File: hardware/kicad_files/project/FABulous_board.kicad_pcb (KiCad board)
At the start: 4 copper layers, 101.2 x 63.5 mm, 87 parts, among them J1 Conn_01x03_Pin, J10 Conn_01x03_Pin, J2 Conn_01x02_Socket, J3 Conn_02x12_Odd_Even, J4 Conn_01x03_Pin, J5 Conn_01x03_Pin, J6 Conn_01x03_Pin, J7 Conn_01x03_Pin, J8 Conn_01x03_Pin, J9 Conn_01x02_Pin, SW1 Tactile Switch, U1 W25Q32FVSS, U10 SN74LVC1G125DCKR, U11 SI5351A-B-GTR, U4 GT-USB-7010ASV, U5 FT232H, U6 AMS1117-3_3, U7 SPX1117M3-L-1-5_TR, U8 MCP1319MT-29LE-OT, U9 SN74LVC1G125DCKR, X1 TXM12M0004252DBCEO00T, X2 NX3225GA-25_000M-STD-CRG-2

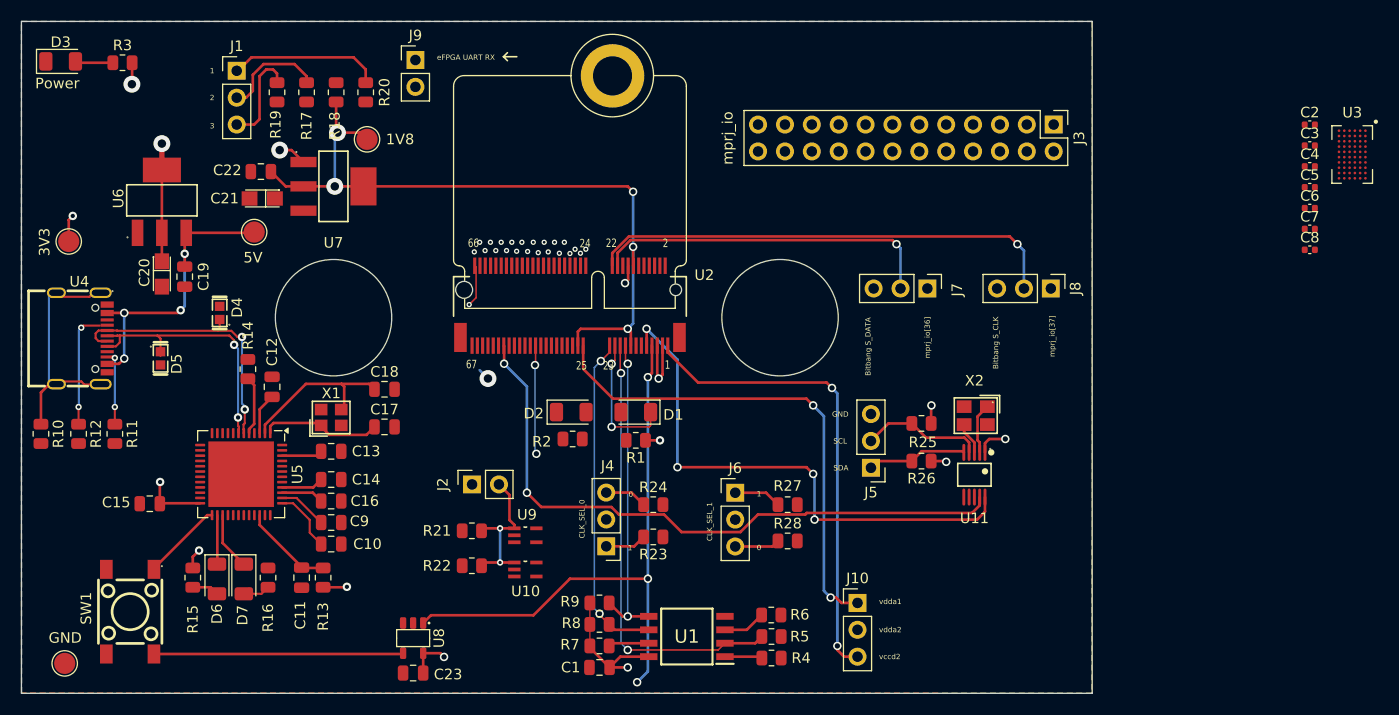
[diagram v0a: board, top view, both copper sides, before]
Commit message: feat: first version of a complete layout. USB-C port might be problematic, FTDI chip does not have the best arrangement
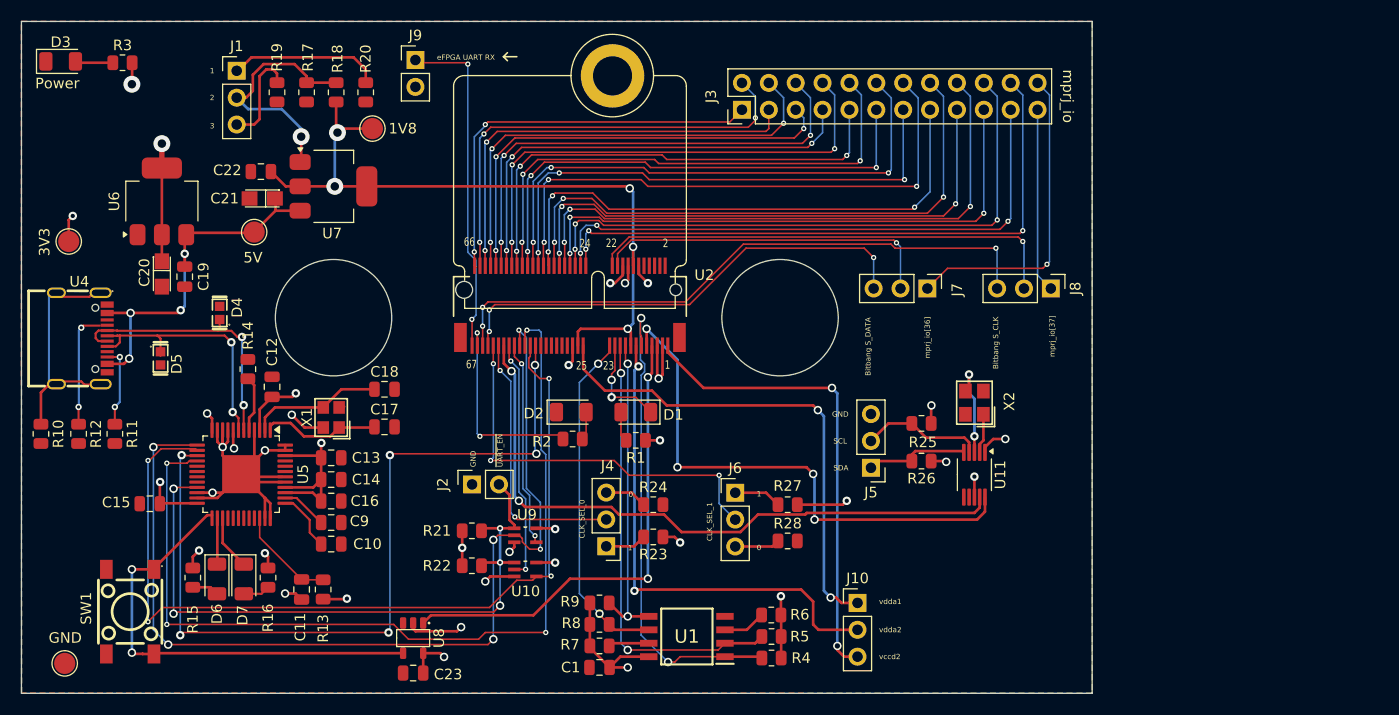
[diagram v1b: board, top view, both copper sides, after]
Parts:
- removed C2, C3, C4, C5, C6, C7, C8: 0.1uF, Capacitor_SMD:C_0402_1005Metric
- removed U3: ~, Caravel_Board:Caravel_WCSP_0_25_mm_bga
- R23, R24, R27, R28: value R -> 10k
- U11: footprint easy_eda:MSOP-10_L3.0-W3.0-P0.50-LS5.0-BL -> Package_SO:MSOP-10_3x3mm_P0.5mm
- U5: footprint Package_DFN_QFN:QFN-48-1EP_8x8mm_P0.5mm_EP6.2x6.2mm -> Package_QFP:LQFP-48-1EP_7x7mm_P0.5mm_EP3.6x3.6mm
- U6: footprint easy_eda:SOT-223-3_L6.5-W3.4-P2.30-LS7.0-BR -> Package_TO_SOT_SMD:SOT-223-3_TabPin2
- U7: footprint easy_eda:SOT-223-4_L6.5-W3.5-P2.30-LS7.0-BR -> Package_TO_SOT_SMD:SOT-223-3_TabPin2
- moved J3 29.5 mm to (171.7, 76.3), turned to 90 degrees
- moved TP2 17.5 mm to (125.6, 87.9), turned to 0 degrees
- moved TP3 17.5 mm to (108.1, 88.8), turned to 0 degrees
- moved X2 1.23 mm to (193.7, 104.0), turned to 90 degrees
- moved TP4 1.14 mm to (136.8, 78.1)
- moved C11 1.12 mm to (130.1, 121.7)
- moved R13 1.12 mm to (132.1, 121.7)
- moved C13 0.61 mm to (132.9, 109.2)
- turned TP1 to 0 degrees
- turned U11 to -90 degrees
- turned U6 to 90 degrees
- turned U7 to 0 degrees
- turned X1 to 90 degrees
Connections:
- net /PC connection/D+ renamed /PC Connection/D+
- net /PC connection/D- renamed /PC Connection/D-
- net /PC connection/Oscillator/OSC1 renamed /PC Connection/Oscillator/OSC1
- net /PC connection/Oscillator/OSC2 renamed /PC Connection/Oscillator/OSC2
- net /PC connection/REF renamed /PC Connection/REF
- net /PC connection/RX_LED renamed /PC Connection/RX_LED
- net /PC connection/Shield renamed /PC Connection/Shield
- net /PC connection/TX_LED renamed /PC Connection/TX_LED
- net /PC connection/VCCA renamed /PC Connection/VCCA
- net /PC connection/VCCCORE renamed /PC Connection/VCCCORE
- net /PC connection/~{MR} renamed /PC Connection/~{MR}
- net /PC connection/~{RESET} renamed /PC Connection/~{RESET}
- net /Power conversion/ADJ renamed /Power Conversion/ADJ
- net /Power conversion/ADJ_1_45 renamed /Power Conversion/ADJ_1_45
- net /Power conversion/ADJ_1_6 renamed /Power Conversion/ADJ_1_6
- TP2 pad 1: +3V3 -> +5V
- TP3 pad 1: +5V -> +3V3
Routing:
- net /FTDI_SPI.SCK: track 0.00 -> 92.2 mm, vias 0 -> 6
- net /FTDI_SPI.CS: track 0.00 -> 86.4 mm, vias 0 -> 4
- net /FTDI_SPI.DI: track 0.00 -> 83.5 mm, vias 0 -> 4
- net GND: track 0.00 -> 70.1 mm, vias 0 -> 12
- net /FTDI_SPI.DO: track 10.3 -> 79.6 mm, vias 2 -> 6
- net /Caravel Connections/mprj_io.35: track 0.00 -> 59.1 mm, vias 1 -> 3
- net /Caravel Connections/Bitbang.S_DATA: track 0.00 -> 58.6 mm, vias 0 -> 3
- net /Caravel Connections/mprj_io.33: track 0.00 -> 57.9 mm, vias 1 -> 3
- net /Caravel Connections/mprj_io.31: track 0.00 -> 56.5 mm, vias 1 -> 3
- net /Caravel Connections/mprj_io.29: track 0.00 -> 55.2 mm, vias 1 -> 3
- net /Caravel Connections/mprj_io.34: track 0.00 -> 55.0 mm, vias 1 -> 3
- net /Caravel Connections/mprj_io.32: track 0.00 -> 54.0 mm, vias 1 -> 3
- net /Caravel Connections/mprj_io.27: track 0.00 -> 53.8 mm, vias 1 -> 3
- net /Caravel Connections/mprj_io.30: track 0.00 -> 52.9 mm, vias 1 -> 3
- net /Caravel Connections/mprj_io.28: track 0.00 -> 51.7 mm, vias 1 -> 3
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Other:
- board text added: "~{UART_EN}"

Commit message: refactor: reposition FTDI and other components to improve routing
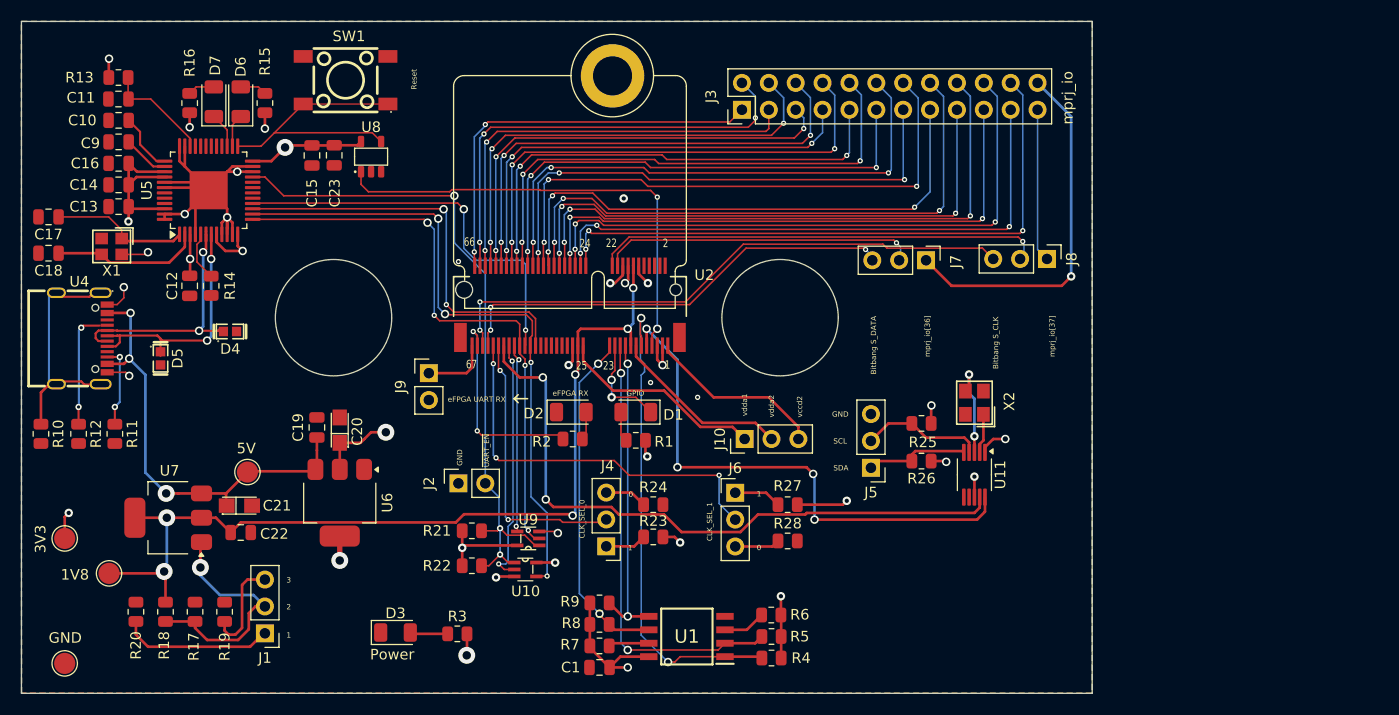
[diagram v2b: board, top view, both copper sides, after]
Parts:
- U10: value SN74LVC1G125DCKR -> (none)
- moved D3 62.6 mm to (139.0, 125.7)
- moved R3 62.6 mm to (144.8, 125.9)
- moved SW1 54.2 mm to (134.2, 73.5), turned to 180 degrees
- moved R20 53.7 mm to (114.4, 123.8), turned to 90 degrees
- moved J1 53.2 mm to (126.6, 125.8), turned to 180 degrees
- moved R13 52.1 mm to (112.8, 73.3), turned to 0 degrees
- moved R18 51.7 mm to (117.2, 123.8), turned to -90 degrees
- moved R17 50.2 mm to (120.0, 123.8), turned to 90 degrees
- moved C23 49.5 mm to (133.2, 80.6), turned to 90 degrees
- moved C11 49.5 mm to (112.8, 75.3), turned to 0 degrees
- moved R19 49.3 mm to (122.8, 123.8), turned to 90 degrees
- moved TP4 48.9 mm to (111.9, 120.1), turned to 180 degrees
- moved U8 45.7 mm to (136.7, 80.8), turned to 90 degrees
- moved R16 45.5 mm to (119.5, 75.7), turned to -90 degrees
- moved R15 45.4 mm to (126.6, 75.7), turned to -90 degrees
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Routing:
- net /FTDI_SPI.CS: track 86.4 -> 38.1 mm, vias 4 -> 2
- net /FTDI_SPI.DO: track 79.6 -> 38.8 mm, vias 6 -> 2
- net /FTDI_SPI.SCK: track 92.2 -> 55.4 mm, vias 6 -> 4
- net /Caravel Connections/vdda2: track 47.4 -> 17.1 mm, vias 2 -> 0
- net /Caravel Connections/vccd2: track 44.7 -> 17.0 mm, vias 2 -> 0
- net /Caravel Connections/vdda1: track 47.0 -> 19.8 mm, vias 2 -> 0
- net /efpga_uart_rx: track 32.2 -> 6.37 mm, vias 2 -> 0
- net /FTDI_SPI.DI: track 83.5 -> 61.4 mm
- net /PC Connection/~{MR}: track 43.5 -> 26.3 mm, vias 2 -> 0
- net +1V8: track 69.4 -> 86.5 mm, vias 5 -> 6
- net +5V: track 35.3 -> 42.5 mm, vias 4 -> 3
- net /Caravel Connections/mprj_io.37: track 30.0 -> 34.7 mm
- net GND: track 70.1 -> 65.5 mm, vias 12 -> 16
- net /Caravel Connections/mprj_io.36: track 17.4 -> 14.5 mm
- net /Caravel Connections/Bitbang.S_CLK: track 45.5 -> 42.8 mm
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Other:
- board text added: "B"
- board text added: "FABul"
- board text added: "GPIO"
- board text added: "Reset"
- board text added: "ard"
- board text added: "eFPGA RX"
- board text added: "pen"

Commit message: feat: optimize layout, reassign annotations, add 2x4 header for UART selection
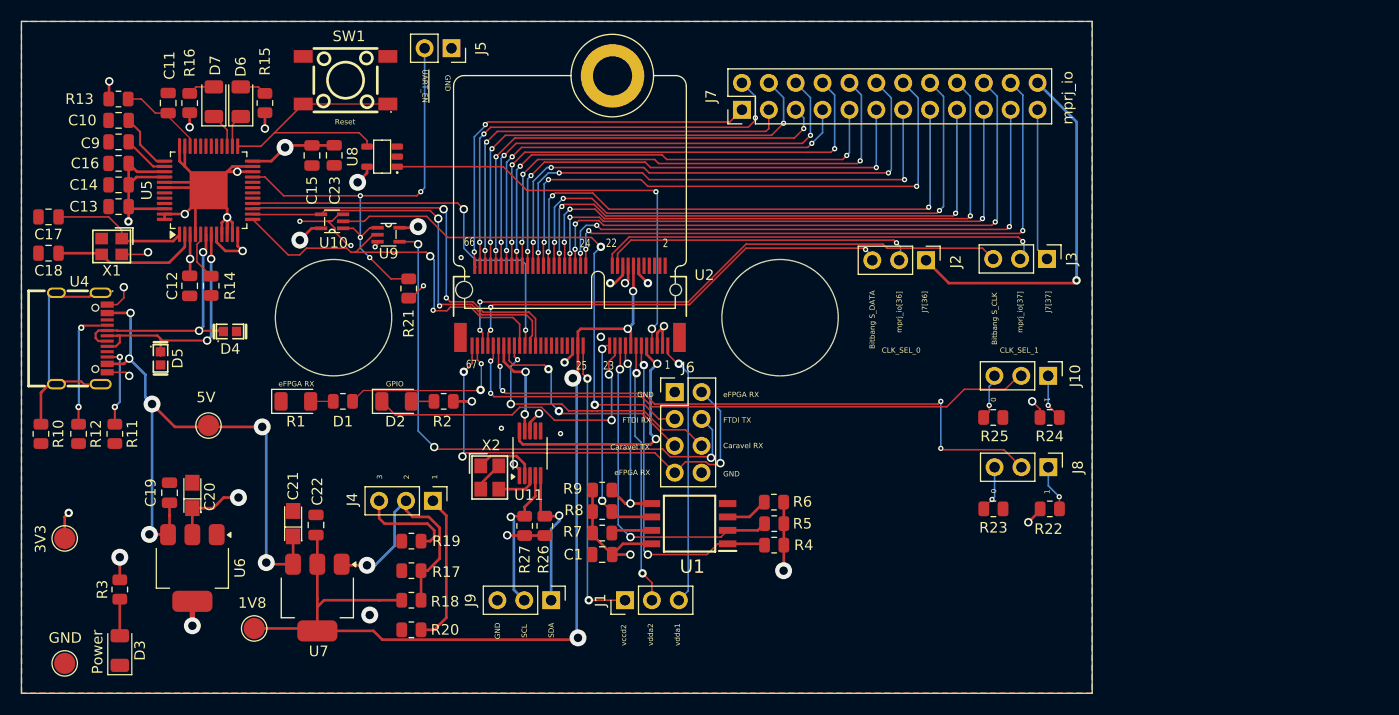
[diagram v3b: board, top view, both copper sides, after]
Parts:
- removed the J9 at (142.1, 101.2)
- removed the R21 at (146.2, 116.1)
- added J6: Conn_02x04_Odd_Even, Connector_PinHeader_2.54mm:PinHeader_2x04_P2.54mm_Vertical, F.Cu at (165.3, 103.0)
- R1: renamed from R2; value 82 -> 82
- R13: value 10k -> 10k
- R14: value 12K -> 12K
- R16: value 150 -> 150
- R2: renamed from R1; value 82 -> 82
- U10: value (none) -> SN74LVC1G125DCKR
- moved X2 46.4 mm to (147.9, 111.1), turned to -90 degrees
- moved J8 42.4 mm to (200.7, 110.1), turned to -90 degrees
- moved U11 42.0 mm to (151.7, 108.8), turned to 90 degrees
- moved J5 41.1 mm to (144.3, 70.5), turned to -90 degrees
- moved R27 38.7 mm to (151.2, 115.7), turned to 90 degrees
- moved U10 37.6 mm to (133.0, 86.9), turned to 180 degrees
- moved R22 37.6 mm to (200.8, 114.0), turned to 0 degrees
- moved R26 36.1 mm to (153.1, 115.7), turned to 90 degrees
- moved J9 32.7 mm to (153.7, 122.7), turned to -90 degrees
- moved R3 32.2 mm to (112.9, 121.7), turned to -90 degrees
- moved R23 32.1 mm to (195.5, 114.0)
- moved U9 31.6 mm to (138.3, 88.1), turned to 0 degrees
- moved J10 31.6 mm to (200.6, 101.5), turned to -90 degrees
- moved R21 26.9 mm to (140.2, 93.2), turned to 90 degrees
- moved D3 26.1 mm to (112.9, 127.4), turned to 90 degrees
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- renumbered D2 to D1, D1 to D2, J10 to J1, J6 to J10, J7 to J2, J8 to J3, J1 to J4, J2 to J5, J3 to J7, J4 to J8, J5 to J9, R22 to R21, R23 to R22, R24 to R23, R27 to R24, R28 to R25, R25 to R27
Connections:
- net Net-(J4-Pin_1) renamed /Pin Headers/CLK_SEL_0_PU
- net Net-(J4-Pin_3) renamed /Pin Headers/CLK_SEL_0_PD
- net Net-(J6-Pin_1) renamed /Pin Headers/CLK_SEL_1_PU
- net Net-(J6-Pin_3) renamed /Pin Headers/CLK_SEL_1_PD
- U10 pad 2: /UART.TX -> /FTDI_UART_RX
- U9 pad 4: /UART.RX -> /FTDI_UART_TX
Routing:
- net /FTDI_UART_TX: track 0.00 -> 52.4 mm, vias 0 -> 3
- net /FC.external_clock: track 61.7 -> 9.59 mm
- net /FTDI_UART_RX: track 0.00 -> 49.3 mm, vias 0 -> 2
- net /efpga_uart_rx: track 6.37 -> 44.2 mm, vias 0 -> 3
- net /FC.clock_select_0: track 26.3 -> 59.3 mm, vias 2 -> 4
- net /CLK_caravel: track 51.2 -> 24.0 mm, vias 4 -> 2
- net /FTDI_SPI.DI: track 61.4 -> 38.2 mm, vias 4 -> 2
- net /Caravel Connections/GPIO: track 9.28 -> 30.4 mm
- net /~{UART_EN}: track 66.1 -> 45.7 mm, vias 3 -> 4
- net /FC.clock_select_1: track 37.3 -> 56.5 mm, vias 3 -> 2
- net +5V: track 42.5 -> 61.0 mm, vias 3 -> 6
- net /FTDI_SPI.SCK: track 55.4 -> 37.9 mm, vias 4 -> 2
- net /Caravel_SPI.CS: track 45.7 -> 31.5 mm
- net /Caravel_SPI.SCK: track 32.7 -> 20.5 mm
- net /Caravel_SPI.DO: track 29.9 -> 19.4 mm
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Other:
- board text added: "Caravel RX"
- board text added: "Caravel TX"
- board text added: "FTDI RX"
- board text added: "FTDI TX"
- board text added: "J7[36]"
- board text added: "J7[37]"
- board text removed: "FABul"
- board text removed: "eFPGA UART RX"

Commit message: feat: implemented all suggestions, logos still missing or incorrect
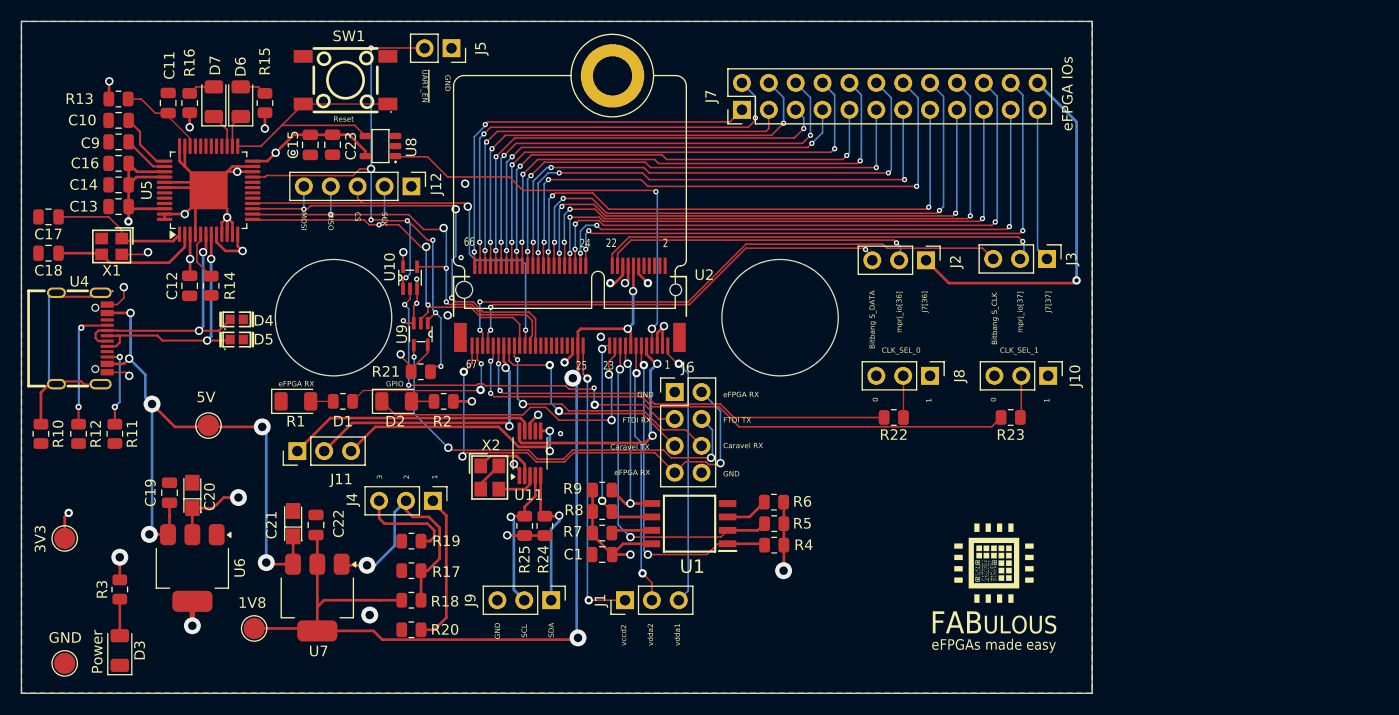
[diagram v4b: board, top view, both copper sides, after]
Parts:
- removed the R24 at (200.8, 105.4)
- removed the R25 at (195.5, 105.4)
- added J11: Conn_01x03_Pin, Connector_PinHeader_2.54mm:PinHeader_1x03_P2.54mm_Vertical, F.Cu at (129.7, 108.6)
- added J12: Conn_01x05_Pin, Connector_PinHeader_2.54mm:PinHeader_1x05_P2.54mm_Vertical, F.Cu at (140.5, 83.6)
- added T1: LOGO, FABulous:fabulous_logo_qr_code_generated, F.Cu at (195.5, 121.3)
- D1: value red -> blue
- D3, D6, D7: value red -> yellow green
- moved R22 17.1 mm to (186.1, 105.4), turned to 180 degrees
- moved J8 14.1 mm to (189.5, 101.5)
- moved U9 9.88 mm to (141.4, 97.5), turned to -90 degrees
- moved U10 9.09 mm to (140.3, 92.2), turned to 90 degrees
- moved R23 8.79 mm to (197.1, 105.4), turned to 180 degrees
- moved R21 7.96 mm to (141.4, 101.1), turned to 0 degrees
- moved D5 7.42 mm to (124.0, 98.0), turned to 0 degrees
- moved D4 1.31 mm to (124.0, 96.1)
- moved C15 1.01 mm to (130.9, 79.6)
- moved C23 1.01 mm to (133.0, 79.6)
- moved U8 1.01 mm to (137.5, 79.8)
- renumbered R26 to R24, R27 to R25
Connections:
- J10 pad 1: /Pin Headers/CLK_SEL_1_PU -> +3V3
- J10 pad 2: /FC.clock_select_1 -> Net-(J10-Pin_2)
- J10 pad 3: /Pin Headers/CLK_SEL_1_PD -> GND
- J8 pad 1: /Pin Headers/CLK_SEL_0_PU -> +3V3
- J8 pad 2: /FC.clock_select_0 -> Net-(J8-Pin_2)
- J8 pad 3: /Pin Headers/CLK_SEL_0_PD -> GND
- R22 pad 1: +3V3 -> Net-(J8-Pin_2)
- R22 pad 2: /Pin Headers/CLK_SEL_0_PU -> /FC.clock_select_0
- R23 pad 1: /Pin Headers/CLK_SEL_0_PD -> Net-(J10-Pin_2)
- R23 pad 2: GND -> /FC.clock_select_1
- U11 pad 6: unconnected-(U11-CLK2-Pad6) -> /CLK_efpga_1
- U11 pad 9: /FC.external_clock -> /CLK_efpga_0
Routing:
- net /CLK_efpga_1: track 0.00 -> 23.4 mm, vias 0 -> 2
- net /CLK_efpga_0: track 0.00 -> 23.0 mm
- net /FC.clock_select_0: track 59.3 -> 41.7 mm, vias 4 -> 2
- net /FC.external_clock: track 9.59 -> 26.6 mm
- net /~{UART_EN}: track 45.7 -> 61.3 mm, vias 4 -> 8
- net /FTDI_UART_RX: track 49.3 -> 37.4 mm, vias 2 -> 4
- net /FTDI_UART_TX: track 52.4 -> 41.1 mm
- net /FTDI_SPI.DI: track 38.2 -> 43.2 mm, vias 2 -> 4
- net /Pin Headers/CLK_SEL_0_PD: track 4.43 -> 0.00 mm, vias 1 -> 0
- net /Pin Headers/CLK_SEL_1_PD: track 4.39 -> 0.00 mm, vias 1 -> 0
- net /Pin Headers/CLK_SEL_0_PU: track 4.37 -> 0.00 mm, vias 1 -> 0
- net /Pin Headers/CLK_SEL_1_PU: track 4.37 -> 0.00 mm, vias 1 -> 0
- net Net-(J10-Pin_2): track 0.00 -> 4.21 mm
- net Net-(J8-Pin_2): track 0.00 -> 3.95 mm
- net /FTDI_SPI.DO: track 38.5 -> 42.2 mm, vias 2 -> 3
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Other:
- board text added: "CS"
- board text added: "MISO"
- board text added: "MOSI"
- board text added: "SCK"
- board text added: "eFPGA IOs"
- board text removed: "mprj_io"
